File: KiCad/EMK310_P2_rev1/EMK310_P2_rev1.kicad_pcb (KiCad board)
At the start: 2 copper layers, 100 x 100 mm, 65 parts, among them J1 Conn_01x20_Socket, J2 Conn_01x02_Socket, J3 Conn_01x02_Socket, J4 Conn_01x20_Socket, J5 Conn_01x05_Socket, J6 Conn_01x04_Socket, U1 PIC18F45K22, U2 Opamp_Quad, U3 Opamp_Dual, U4 MCP2221AxP

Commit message: Updated PCB Design
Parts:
- removed D1, D2, D3, D4, D5: LED_BGKR, LED_THT:LED_D5.0mm-4_RGB_Wide_Pins
- removed D10, D6, D7, D8, D9: D_Photo, LED_THT:LED_D5.0mm
- removed R1, R10, R11, R12, R13, R14, R15, R2, R3, R4, R5, R6, R7, R8, R9: R, Resistor_THT:R_Axial_DIN0207_L6.3mm_D2.5mm_P10.16mm_Horizontal
- removed U4: MCP2221AxP, Package_DIP:DIP-14_W7.62mm
- removed Wf1: Conn_02x04_Counter_Clockwise, Connector_PinHeader_2.54mm:PinHeader_2x04_P2.54mm_Vertical
- added J7: Conn_01x02_Socket, Connector_PinHeader_2.54mm:PinHeader_1x02_P2.54mm_Vertical, F.Cu at (101.2, 57.2)
- added RF1: ESP-01-Wifi, Jan-Hendrik:PinHeader_2x04_P2.54mm_Vertical_Antenna, F.Cu at (172.8, 46.2)
- moved R29 24.7 mm to (102.8, 93.7), turned to -90 degrees
- moved C5 12.0 mm to (110.5, 54.2), turned to 90 degrees
- moved R30 7.41 mm to (107.2, 93.8), turned to -90 degrees
- moved PR1 5.84 mm to (101.2, 51.2)
- moved J2 3.13 mm to (172.5, 62.8)
- moved J3 3.13 mm to (172.5, 69.2)
- moved J6 3.01 mm to (132.6, 46.8)
- moved AFF1 2.76 mm to (99.7, 90.4)
- moved C1 2.76 mm to (144.8, 46.8)
- moved C2 2.76 mm to (144.8, 49.8)
- moved C3 2.76 mm to (150.2, 86.2)
- moved C4 2.76 mm to (150.2, 89.2)
- moved J1 2.76 mm to (168.2, 80.2)
- moved J4 2.76 mm to (168.1, 54.2)
- moved J5 2.76 mm to (103.5, 121.1)
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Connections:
- AFF1 pad 5: unconnected-(AFF1-DP-Pad5) -> GNDREF
- J1 pad 8: /MOTOR_2_F -> Net-(J1-Pin_8)
- J4 pad 10: /MOTOR_1_B -> /MOTOR_1_F
- J4 pad 20: Net-(J4-Pin_20) -> /MOTOR_1_B
- J4 pad 8: /MOTOR_1_F -> /MOTOR_2_F
- J5 pad 3: Net-(D8-A) -> Net-(D10-A)
- J5 pad 4: Net-(D9-A) -> Net-(D8-A)
- J5 pad 5: Net-(D10-A) -> Net-(D9-A)
- J6 pad 4: Net-(D1-K) -> GNDREF
- R26 pad 2: Net-(J1-Pin_12) -> Net-(J1-Pin_11)
- R27 pad 2: Net-(J1-Pin_13) -> Net-(J1-Pin_12)
- R28 pad 2: Net-(J1-Pin_14) -> Net-(J1-Pin_13)
- R29 pad 2: Net-(J1-Pin_19) -> Net-(J1-Pin_14)
- R30 pad 2: Net-(J1-Pin_20) -> Net-(J1-Pin_19)
- R31 pad 2: Net-(J4-Pin_20) -> Net-(J1-Pin_20)
- U1 pad 10: /MOTOR_1_B -> /MOTOR_1_F
- U1 pad 20: Net-(J4-Pin_20) -> /MOTOR_1_B
- U1 pad 33: /MOTOR_2_F -> Net-(J1-Pin_8)
- U1 pad 8: /MOTOR_1_F -> /MOTOR_2_F
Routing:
- net /Vdd: track 0.00 -> 138.4 mm, vias 0 -> 2
- net Net-(J4-Pin_18): track 0.00 -> 79.0 mm, vias 0 -> 2
- net Net-(J1-Pin_16): track 0.00 -> 70.2 mm, vias 0 -> 2
- net Net-(J1-Pin_13): track 0.00 -> 68.7 mm, vias 0 -> 2
- net Net-(J1-Pin_14): track 0.00 -> 63.5 mm, vias 0 -> 2
- net Net-(D10-A): track 0.75 -> 60.6 mm
- net Net-(J1-Pin_15): track 0.00 -> 57.2 mm, vias 0 -> 2
- net Net-(J1-Pin_11): track 0.00 -> 55.7 mm, vias 0 -> 2
- net Net-(J1-Pin_12): track 0.00 -> 51.4 mm, vias 0 -> 4
- net Net-(D9-A): track 0.00 -> 48.9 mm
- net Net-(D6-A): track 0.00 -> 48.9 mm
- net Net-(J1-Pin_17): track 0.00 -> 46.9 mm, vias 0 -> 6
- net Net-(J1-Pin_18): track 0.00 -> 46.9 mm, vias 0 -> 4
- net Net-(D8-A): track 0.00 -> 44.1 mm
- net Net-(J1-Pin_19): track 0.00 -> 40.1 mm
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- added copper zone on B.Cu, net GNDREF
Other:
- board size 100 x 100 mm -> 80 x 100 mm
- board text added: "Jan-Hendrik Brink 23694956 Group 55"

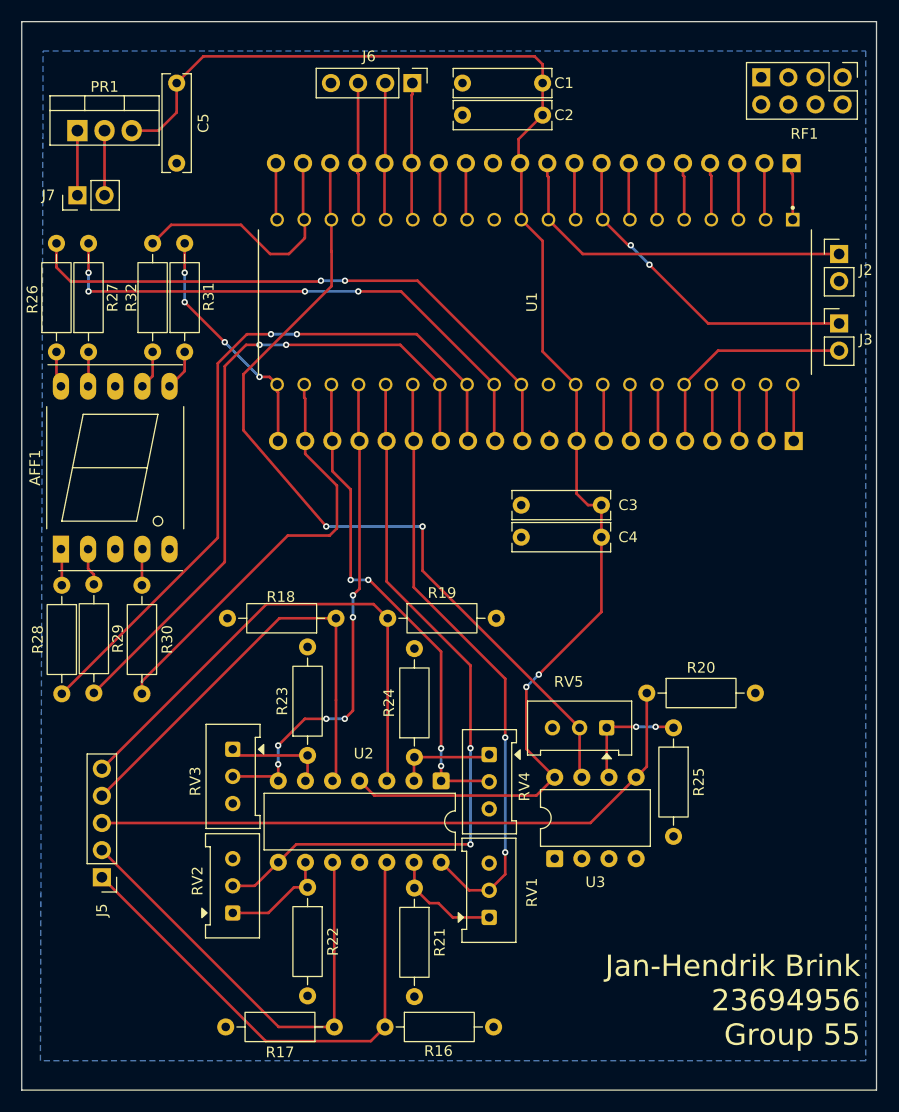
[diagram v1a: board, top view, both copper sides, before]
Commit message: Added mounting Holes to PCB design
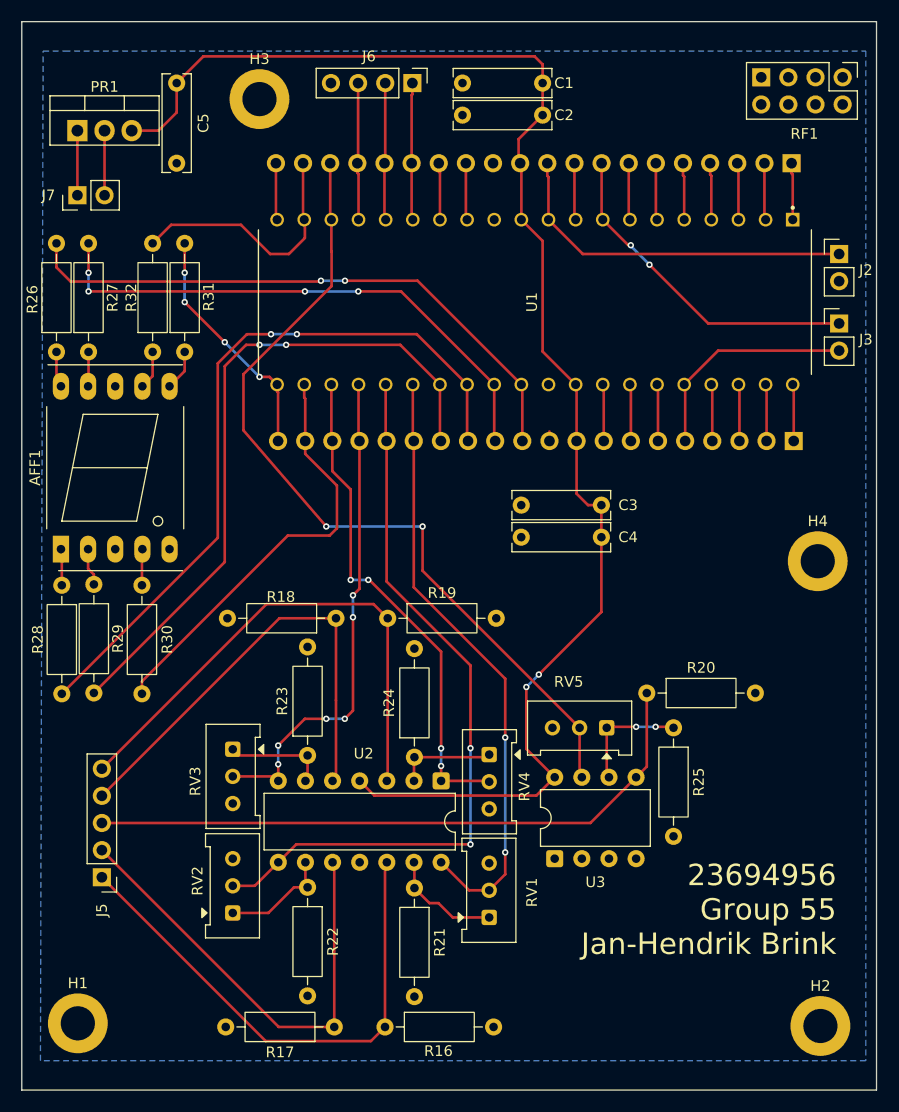
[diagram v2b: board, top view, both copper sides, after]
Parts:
- added H1: MountingHole_Pad, MountingHole:MountingHole_3.2mm_M3_DIN965_Pad, F.Cu at (101.2, 134.8)
- added H2: MountingHole_Pad, MountingHole:MountingHole_3.2mm_M3_DIN965_Pad, F.Cu at (170.8, 135.0)
- added H3: MountingHole_Pad, MountingHole:MountingHole_3.2mm_M3_DIN965_Pad, F.Cu at (118.2, 48.2)
- added H4: MountingHole_Pad, MountingHole:MountingHole_3.2mm_M3_DIN965_Pad, F.Cu at (170.5, 91.5)
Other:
- board text added: "23694956 Group 55 Jan-Hendrik Brink"
- board text removed: "Jan-Hendrik Brink 23694956 Group 55"

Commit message: work
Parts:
- removed RF1: ESP-01-Wifi, Jan-Hendrik:PinHeader_2x04_P2.54mm_Vertical_Antenna
- added C6: 0.22uF, Capacitor_THT:C_Rect_L9.0mm_W2.5mm_P7.50mm_MKT, F.Cu at (165.0, 48.8)
- added C7: 0.22uF, Capacitor_THT:C_Rect_L9.0mm_W2.5mm_P7.50mm_MKT, F.Cu at (153.5, 91.8)
- added C8: 0.22uF, Capacitor_THT:C_Rect_L9.0mm_W2.5mm_P7.50mm_MKT, F.Cu at (107.5, 54.8)
- added J8: USB_A, Connector_USB:USB_A_Connfly_DS1095, F.Cu at (159.5, 47.2)
- added Q1: VP0610L, Package_TO_SOT_THT:TO-92L_Inline, F.Cu at (133.2, 50.8)
- added Q2: VP0610L, Package_TO_SOT_THT:TO-92L_Inline, F.Cu at (127.5, 50.8)
- added Q3: VP0610L, Package_TO_SOT_THT:TO-92L_Inline, F.Cu at (121.5, 50.8)
- added R33: 10k, Resistor_THT:R_Axial_DIN0207_L6.3mm_D2.5mm_P10.16mm_Horizontal, F.Cu at (169.8, 107.5)
- added R34: 10k, Resistor_THT:R_Axial_DIN0207_L6.3mm_D2.5mm_P10.16mm_Horizontal, F.Cu at (172.2, 100.5)
- added R35: 10k, Resistor_THT:R_Axial_DIN0207_L6.3mm_D2.5mm_P10.16mm_Horizontal, F.Cu at (171.2, 66.0)
- added U4: MCP2221AxP, Package_DIP:DIP-14_W7.62mm, F.Cu at (172.2, 90.0)
- C5: value C_Small -> 10uF
- H1, H2, H3, H4: footprint MountingHole:MountingHole_3.2mm_M3_DIN965_Pad -> MountingHole:MountingHole_2.2mm_M2_DIN965_Pad_TopOnly
- moved H4 46.8 mm to (171.2, 44.8)
- moved H3 17.6 mm to (101.0, 45.0)
- moved J2 10.5 mm to (171.5, 73.2)
- moved J3 10.5 mm to (171.5, 79.7)
- moved C3 4.95 mm to (146.8, 89.8)
- moved C4 4.95 mm to (146.8, 92.8)
- moved J6 3.02 mm to (129.8, 45.5)
- moved J1 2.24 mm to (167.2, 82.2)
- moved J4 2.24 mm to (167.1, 56.2)
- moved U1 2.24 mm to (143.0, 69.2)
- moved J7 2.07 mm to (101.7, 59.2)
- moved H2 1.03 mm to (171.8, 135.2)
- moved AFF1 0.84 mm to (100.2, 91.0)
- moved R26 0.84 mm to (99.8, 72.6)
- moved R27 0.84 mm to (102.8, 72.6)
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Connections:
- net Net-(J1-Pin_6) renamed /SDA
- J4 pad 19: Net-(J4-Pin_19) -> /SCL
- J6 pad 1: /LEDR -> Net-(J6-Pin_1)
- J6 pad 2: /LEDG -> Net-(J6-Pin_2)
- J6 pad 3: /LEDB -> Net-(J6-Pin_3)
- R26 pad 2: Net-(J1-Pin_11) -> Net-(J4-Pin_14)
- R27 pad 2: Net-(J1-Pin_12) -> Net-(J4-Pin_7)
- R28 pad 2: Net-(J1-Pin_13) -> Net-(J4-Pin_6)
- R29 pad 2: Net-(J1-Pin_14) -> Net-(J4-Pin_5)
- R30 pad 2: Net-(J1-Pin_19) -> Net-(J4-Pin_4)
- R31 pad 2: Net-(J1-Pin_20) -> Net-(J4-Pin_3)
- R32 pad 2: Net-(J4-Pin_19) -> Net-(J4-Pin_2)
- U1 pad 19: Net-(J4-Pin_19) -> /SCL
- U3 pad 1: unconnected-(U3-Pad1) -> Net-(U3A--)
- U3 pad 2: unconnected-(U3A---Pad2) -> Net-(U3A--)
- U3 pad 3: unconnected-(U3A-+-Pad3) -> GNDREF
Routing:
- net /SCL: track 0.00 -> 115.3 mm, vias 0 -> 5
- net /Vdd: track 138.4 -> 246.0 mm, vias 2 -> 1
- net Net-(J4-Pin_5): track 5.33 -> 97.6 mm, vias 0 -> 4
- net Net-(J4-Pin_6): track 5.33 -> 96.9 mm, vias 0 -> 4
- net Net-(J4-Pin_4): track 5.33 -> 94.3 mm, vias 0 -> 4
- net Net-(J4-Pin_2): track 5.33 -> 76.4 mm, vias 0 -> 4
- net Net-(J8-D+): track 0.00 -> 70.1 mm
- net Net-(J8-D-): track 0.00 -> 67.5 mm
- net Net-(J4-Pin_3): track 5.33 -> 71.7 mm, vias 0 -> 4
- net Net-(J1-Pin_13): track 68.7 -> 5.32 mm, vias 2 -> 0
- net Net-(J4-Pin_7): track 5.33 -> 65.1 mm, vias 0 -> 6
- net /MOTOR_1_B: track 5.33 -> 63.8 mm, vias 0 -> 2
- net Net-(J1-Pin_14): track 63.5 -> 5.32 mm, vias 2 -> 0
- net /SDA: track 5.32 -> 58.5 mm, vias 0 -> 1
- net Net-(J4-Pin_14): track 5.33 -> 47.0 mm, vias 0 -> 4
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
